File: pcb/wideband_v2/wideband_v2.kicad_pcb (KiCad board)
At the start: 2 copper layers, 50 x 40 mm, 103 parts, among them J1 DISPLAY, J2 GPIO, J3 LSU, J4 Tag connect, J5 USB, Q1 BTS3028, SW1 SW_Push, U1 MCP4725xxx-xCH, U10 XC6206P332MR, U2 L7805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

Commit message: Updating BOM SKUs
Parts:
- D4: value BLUE -> RED
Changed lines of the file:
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@@
     (descr "Resistor SMD 0603 (1608 Metric), square (rectangular) end terminal, IPC_7351 nominal, (Body size source: IPC-SM-782 page 72, https://www.pcb-3d.com/wordpress/wp-content/uploads/ipc-sm-782a_amendment_1_and_2.pdf), generated with kicad-footprint-generator")
     (tags "resistor")
-    (property "LCSC" "C11702")
     (property "Sheetfile" "wideband_v2.kicad_sch")
     (property "Sheetname" "")
@@
     (property "Sheetfile" "wideband_v2.kicad_sch")
     (property "Sheetname" "")
-    (attr through_hole)
+    (attr through_hole exclude_from_pos_files exclude_from_bom)
     (fp_text reference "J5" (at 0 -2.06 90) (layer "F.SilkS") hide
       (effects (font (size 1 1) (thickness 0.15)))
@@
     (property "Sheetfile" "wideband_v2.kicad_sch")
     (property "Sheetname" "")
-    (attr exclude_from_pos_files)
+    (attr exclude_from_pos_files exclude_from_bom)
     (fp_text reference "H3" (at 0 -3.2) (layer "F.SilkS") hide
       (effects (font (size 1 1) (thickness 0.15)))
@@
     (descr "Resistor SMD 0603 (1608 Metric), square (rectangular) end terminal, IPC_7351 nominal, (Body size source: IPC-SM-782 page 72, https://www.pcb-3d.com/wordpress/wp-content/uploads/ipc-sm-782a_amendment_1_and_2.pdf), generated with kicad-footprint-generator")
     (tags "resistor")
-    (property "LCSC" "C11702")
     (property "Sheetfile" "wideband_v2.kicad_sch")
     (property "Sheetname" "")
@@
     (property "Sheetfile" "wideband_v2.kicad_sch")
     (property "Sheetname" "")
-    (attr exclude_from_pos_files)
+    (attr exclude_from_pos_files exclude_from_bom)
     (fp_text reference "H1" (at 0 -3.2) (layer "F.SilkS") hide
       (effects (font (size 1 1) (thickness 0.15)))
@@
       (effects (font (size 1 1) (thickness 0.15)))
     )
-    (fp_text value "BLUE" (at 0 1.43) (layer "F.Fab")
+    (fp_text value "RED" (at 0 1.43) (layer "F.Fab")
       (effects (font (size 1 1) (thickness 0.15)))
     )
@@
     (property "Sheetfile" "wideband_v2.kicad_sch")
     (property "Sheetname" "")
-    (attr exclude_from_pos_files)
+    (attr exclude_from_pos_files exclude_from_bom)
     (fp_text reference "JP4" (at 0 -1.8 90) (layer "F.SilkS") hide
       (effects (font (size 1 1) (thickness 0.15)))
@@
     (property "Sheetfile" "wideband_v2.kicad_sch")
     (property "Sheetname" "")
-    (attr through_hole)
+    (attr through_hole exclude_from_pos_files exclude_from_bom)
     (fp_text reference "J1" (at 0 -2.33 90) (layer "F.SilkS") hide
       (effects (font (size 1 1) (thickness 0.15)))
@@
     (property "Sheetfile" "wideband_v2.kicad_sch")
     (property "Sheetname" "")
-    (attr through_hole)
+    (attr through_hole exclude_from_pos_files exclude_from_bom)
     (fp_text reference "J2" (at 0 -2.06 90) (layer "F.SilkS") hide
       (effects (font (size 1 1) (thickness 0.15)))
@@
     (property "Sheetfile" "wideband_v2.kicad_sch")
     (property "Sheetname" "")
-    (attr exclude_from_pos_files)
+    (attr exclude_from_pos_files exclude_from_bom)
     (fp_text reference "H2" (at 0 -3.2) (layer "F.SilkS") hide
       (effects (font (size 1 1) (thickness 0.15)))
@@
     (property "Sheetfile" "wideband_v2.kicad_sch")
     (property "Sheetname" "")
-    (attr exclude_from_pos_files)
+    (attr exclude_from_pos_files exclude_from_bom)
     (fp_text reference "H4" (at 0 -3.2) (layer "F.SilkS") hide
       (effects (font (size 1 1) (thickness 0.15)))
@@
     (descr "Resistor SMD 0603 (1608 Metric), square (rectangular) end terminal, IPC_7351 nominal, (Body size source: IPC-SM-782 page 72, https://www.pcb-3d.com/wordpress/wp-content/uploads/ipc-sm-782a_amendment_1_and_2.pdf), generated with kicad-footprint-generator")
     (tags "resistor")
-    (property "LCSC" "C11702")
     (property "Sheetfile" "wideband_v2.kicad_sch")
     (property "Sheetname" "")
@@
     (property "Sheetfile" "wideband_v2.kicad_sch")
     (property "Sheetname" "")
-    (attr exclude_from_pos_files)
+    (attr exclude_from_pos_files exclude_from_bom)
     (fp_text reference "J4" (at 0 -2.7 90) (layer "B.SilkS") hide
       (effects (font (size 1 1) (thickness 0.15)) (justify mirror))
@@
     (property "Sheetfile" "wideband_v2.kicad_sch")
     (property "Sheetname" "")
-    (attr exclude_from_pos_files)
+    (attr exclude_from_pos_files exclude_from_bom)
     (fp_text reference "JP3" (at -2.3 -0.025 90) (layer "B.SilkS")
       (effects (font (size 0.8 0.8) (thickness 0.15)) (justify mirror))
@@
     (property "Sheetfile" "wideband_v2.kicad_sch")
     (property "Sheetname" "")
-    (attr exclude_from_pos_files)
+    (attr exclude_from_pos_files exclude_from_bom)
     (fp_text reference "JP2" (at -2.3 -0.025 90) (layer "B.SilkS")
       (effects (font (size 0.8 0.8) (thickness 0.15)) (justify mirror))
@@
     (property "Sheetfile" "wideband_v2.kicad_sch")
     (property "Sheetname" "")
-    (attr exclude_from_pos_files)
+    (attr exclude_from_pos_files exclude_from_bom)
     (fp_text reference "JP1" (at -2.3 -0.025 90) (layer "B.SilkS")
       (effects (font (size 0.8 0.8) (thickness 0.15)) (justify mirror))

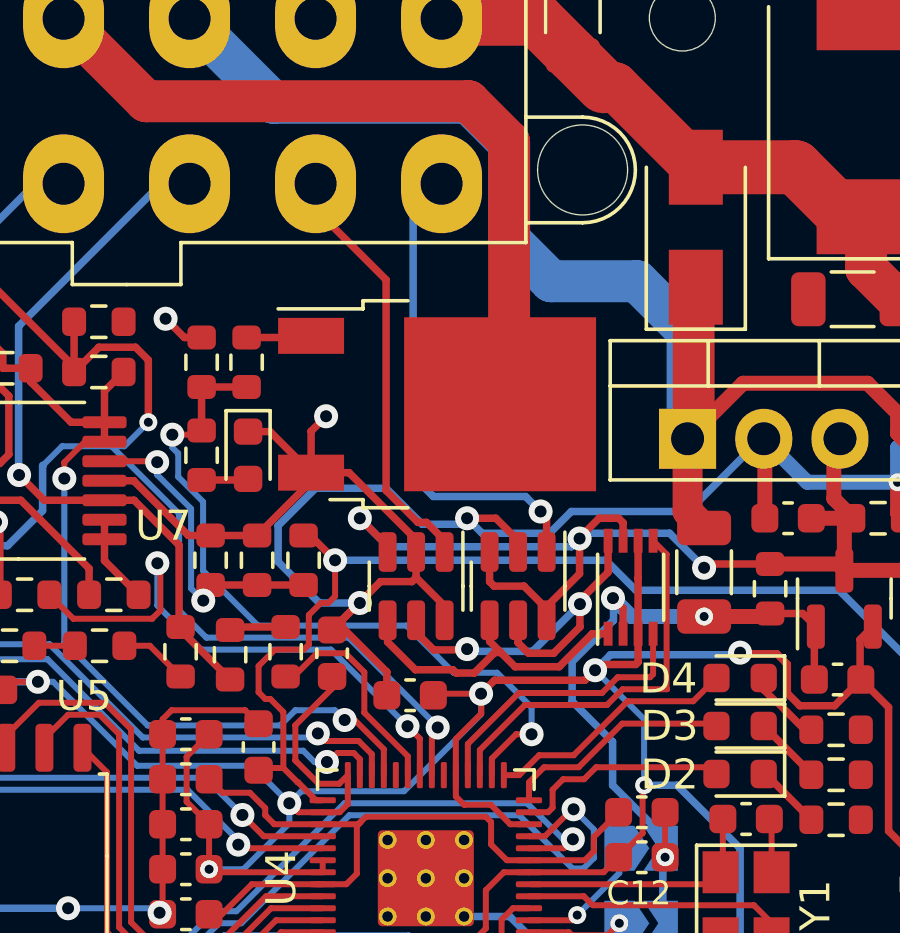
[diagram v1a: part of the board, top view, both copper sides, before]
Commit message: MCP4725 => DAC5571
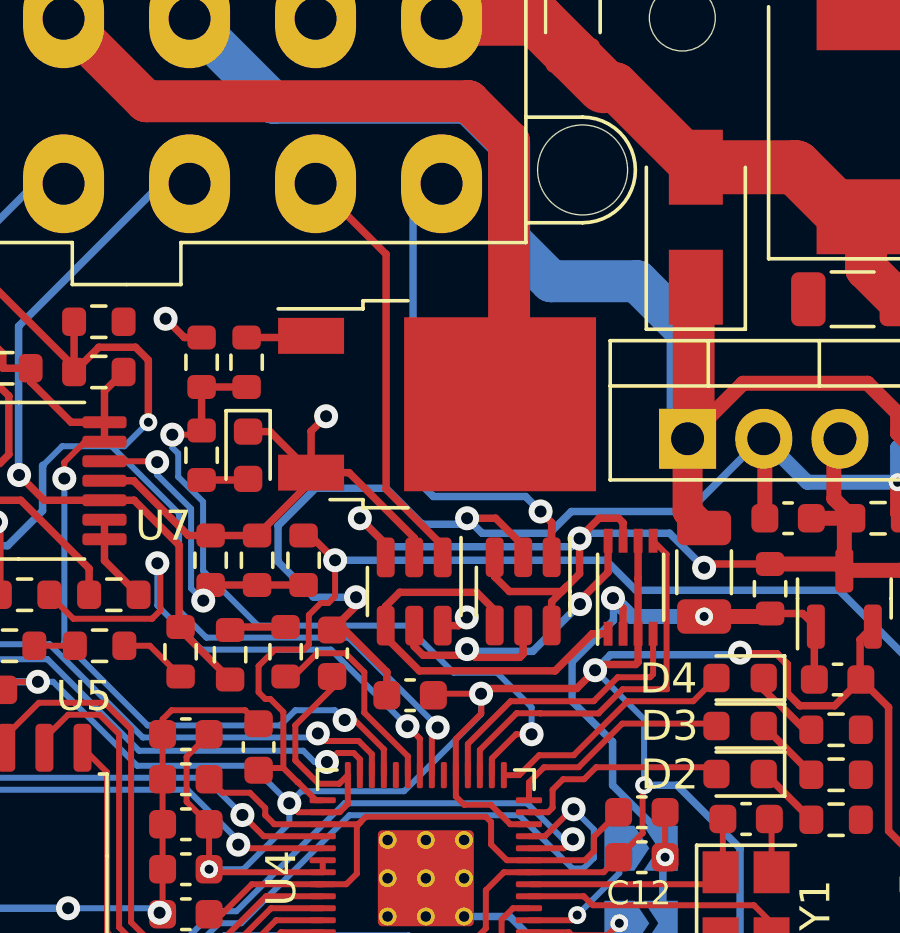
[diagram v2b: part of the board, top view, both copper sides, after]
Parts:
- U1, U3: value MCP4725xxx-xCH -> DAC5571IDBVR
- moved U3 0.24 mm to (136.2, 59.8)
- moved U1 0.19 mm to (132.5, 59.8)
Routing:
- net GND: track 196.9 -> 192.4 mm, vias 16 -> 17
- net /D_SDA_5: track 10.7 -> 14.0 mm
- net /D_SCL_5: track 13.4 -> 12.6 mm
